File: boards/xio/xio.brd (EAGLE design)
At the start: 170 x 170 mm, 249 parts, among them CN3 J00-0065NL, U2 LAN8742A-CZ, X2 USB-A, Y1 NX3225SA-12.000MHZ-STD-CSR-1, Y2 NX3225SA-12.000MHZ-STD-CSR-1, Y3 NX3225SA-25.000MHZ-STD-CSR-1

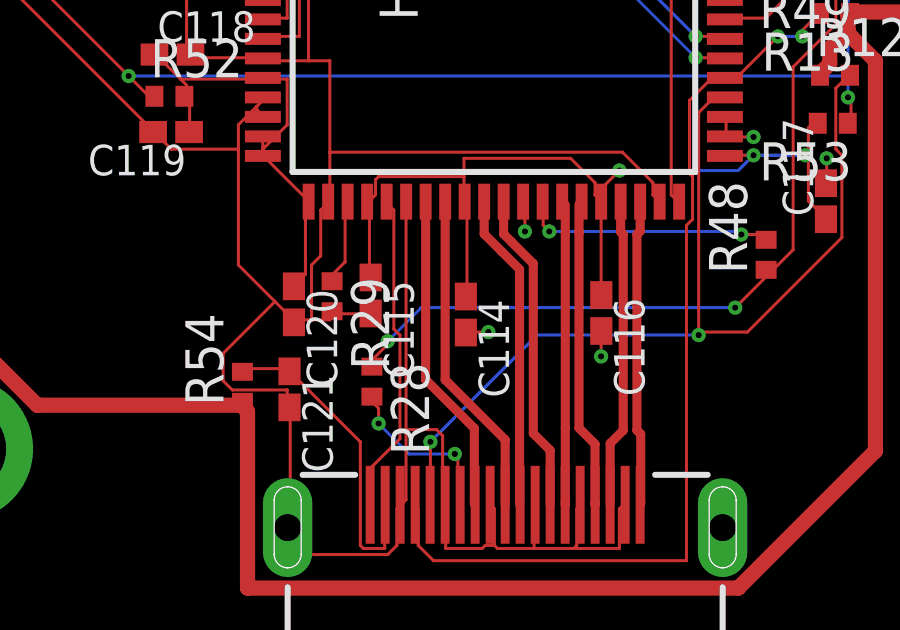
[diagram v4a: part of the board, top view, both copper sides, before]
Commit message: Re-route a diff-pair to be better matched
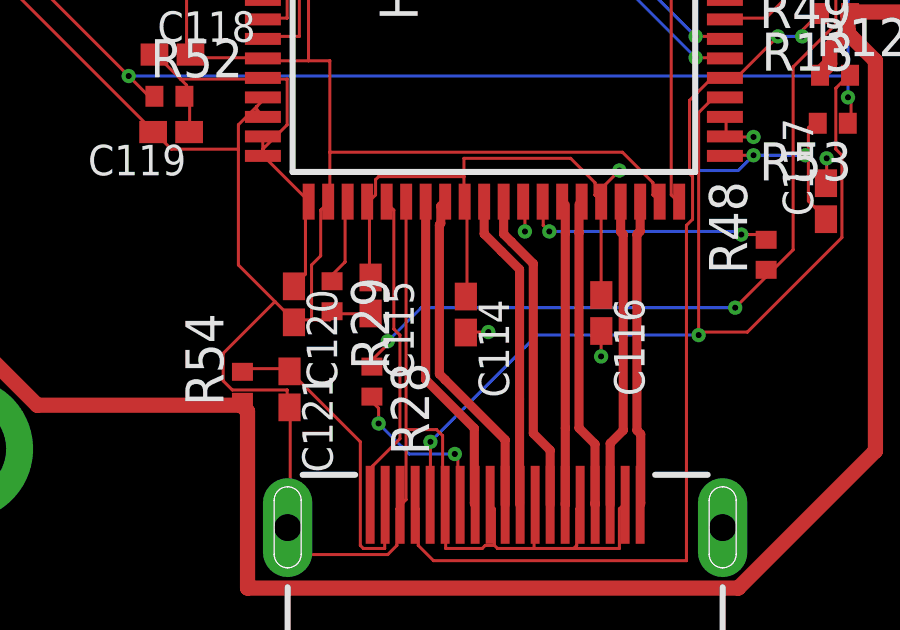
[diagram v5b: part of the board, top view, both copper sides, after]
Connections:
- net N$105 renamed XIO_RAM_A17
- net N$106 renamed XIO_RAM_A18
- net N$107 renamed XIO_RAM_D0
- net N$108 renamed XIO_RAM_D1
- net N$109 renamed XIO_RAM_D2
- net N$110 renamed XIO_RAM_D3
- net N$111 renamed XIO_RAM_D4
- net N$112 renamed XIO_RAM_D5
- net N$113 renamed XIO_RAM_D6
- net N$114 renamed XIO_RAM_D7
- net N$115 renamed XIO_RAM_D8
- net N$116 renamed XIO_RAM_D9
- net N$117 renamed XIO_RAM_D10
- net N$118 renamed XIO_RAM_D11
- net N$119 renamed XIO_RAM_D12
- net N$120 renamed XIO_RAM_D13
- net N$121 renamed XIO_RAM_D14
- net N$122 renamed XIO_RAM_D15
- net N$123 renamed XIO_RAM_!OE!
- net N$124 renamed XIO_RAM_!WE!
- net N$125 renamed XIO_RAM_!LB!
- net N$126 renamed XIO_RAM_!UB!
- net N$127 renamed XIO_RAM_!CS!
- net N$19 renamed XIO_RAM_A0
- net N$22 renamed XIO_RAM_A1
- net N$51 renamed XIO_RAM_A2
- net N$53 renamed XIO_RAM_A3
- net N$54 renamed XIO_RAM_A4
- net N$55 renamed XIO_RAM_A5
- net N$56 renamed XIO_RAM_A6
- net N$57 renamed XIO_RAM_A7
- net N$58 renamed XIO_RAM_A8
- net N$59 renamed XIO_RAM_A9
- net N$60 renamed XIO_RAM_A10
- net N$61 renamed XIO_RAM_A11
- net N$63 renamed XIO_RAM_A12
- net N$65 renamed XIO_RAM_A13
- net N$66 renamed XIO_RAM_A14
- net N$72 renamed XIO_RAM_A15
- net N$73 renamed XIO_RAM_A16

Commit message: Last minute changes prior to review
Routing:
- net +5V: vias 76 -> 92
- added copper zone on layer 1, net +5V
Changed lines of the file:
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@@
 <setting verticaltext="up"/>
 </settings>
-<grid distance="1" unitdist="mil" unit="mil" style="lines" multiple="1" display="yes" altdistance="5" altunitdist="mil" altunit="mil"/>
+<grid distance="0.025" unitdist="inch" unit="inch" style="lines" multiple="1" display="yes" altdistance="5" altunitdist="mil" altunit="mil"/>
 <layers>
 <layer number="1" name="Top" color="4" fill="1" visible="yes" active="yes"/>
@@
 <wire x1="49.5808" y1="84.4296" x2="49.53" y2="84.42" width="0.1016" layer="1"/>
 <wire x1="58.42" y1="84.4296" x2="58.42" y2="84.42" width="0.1016" layer="1"/>
-<wire x1="36.9824" y1="8.7376" x2="36.8808" y2="8.8392" width="0.1016" layer="1"/>
-<wire x1="36.9824" y1="7.5184" x2="36.9824" y2="8.7376" width="0.1016" layer="1"/>
-<wire x1="37.084" y1="7.4168" x2="36.9824" y2="7.5184" width="0.1016" layer="1"/>
-<wire x1="38.3032" y1="7.4168" x2="37.084" y2="7.4168" width="0.1016" layer="1"/>
-<wire x1="38.3032" y1="8.8392" x2="38.3032" y2="7.4168" width="0.1016" layer="1"/>
+<wire x1="36.8808" y1="8.7376" x2="36.8808" y2="8.8392" width="0.1016" layer="1"/>
+<wire x1="36.8808" y1="7.5184" x2="36.8808" y2="8.7376" width="0.1016" layer="1"/>
+<wire x1="37.084" y1="7.3152" x2="36.8808" y2="7.5184" width="0.1016" layer="1"/>
+<wire x1="38.3032" y1="7.3152" x2="37.084" y2="7.3152" width="0.1016" layer="1"/>
+<wire x1="38.3032" y1="8.8392" x2="38.3032" y2="7.3152" width="0.1016" layer="1"/>
 <wire x1="36.8808" y1="8.8392" x2="36.8399" y2="8.8721" width="0.1016" layer="1"/>
 <wire x1="38.3032" y1="8.8392" x2="38.3399" y2="8.8721" width="0.1016" layer="1"/>
-<wire x1="39.7256" y1="8.7376" x2="39.8272" y2="8.8392" width="0.1016" layer="1"/>
-<wire x1="39.7256" y1="7.5184" x2="39.7256" y2="8.7376" width="0.1016" layer="1"/>
-<wire x1="39.624" y1="7.4168" x2="39.7256" y2="7.5184" width="0.1016" layer="1"/>
-<wire x1="38.3032" y1="7.4168" x2="39.624" y2="7.4168" width="0.1016" layer="1"/>
+<wire x1="39.8272" y1="8.7376" x2="39.8272" y2="8.8392" width="0.1016" layer="1"/>
+<wire x1="39.8272" y1="7.5184" x2="39.8272" y2="8.7376" width="0.1016" layer="1"/>
+<wire x1="39.8272" y1="7.3152" x2="39.8272" y2="7.5184" width="0.1016" layer="1"/>
+<wire x1="38.3032" y1="7.3152" x2="39.8272" y2="7.3152" width="0.1016" layer="1"/>
 <wire x1="39.8272" y1="8.8392" x2="39.8399" y2="8.8721" width="0.1016" layer="1"/>
-<wire x1="41.148" y1="8.7376" x2="41.2496" y2="8.8392" width="0.1016" layer="1"/>
-<wire x1="41.148" y1="7.4168" x2="41.148" y2="8.7376" width="0.1016" layer="1"/>
-<wire x1="39.624" y1="7.4168" x2="41.148" y2="7.4168" width="0.1016" layer="1"/>
+<wire x1="41.2496" y1="8.7376" x2="41.2496" y2="8.8392" width="0.1016" layer="1"/>
+<wire x1="41.2496" y1="7.3152" x2="41.2496" y2="8.7376" width="0.1016" layer="1"/>
+<wire x1="39.8272" y1="7.3152" x2="41.2496" y2="7.3152" width="0.1016" layer="1"/>
 <wire x1="41.2496" y1="8.8392" x2="41.3399" y2="8.8721" width="0.1016" layer="1"/>
 <wire x1="34.036" y1="9.0424" x2="34.036" y2="11.3792" width="0.1016" layer="1"/>
@@
 <wire x1="34.036" y1="11.3792" x2="35.052" y2="11.3792" width="0.1016" layer="1"/>
 <wire x1="35.2552" y1="8.9408" x2="35.3399" y2="8.8721" width="0.1016" layer="1"/>
-<wire x1="36.6776" y1="7.5184" x2="36.9824" y2="7.5184" width="0.1016" layer="1"/>
-<wire x1="36.576" y1="7.4168" x2="36.6776" y2="7.5184" width="0.1016" layer="1"/>
-<wire x1="35.3568" y1="7.4168" x2="36.576" y2="7.4168" width="0.1016" layer="1"/>
-<wire x1="35.3568" y1="8.8392" x2="35.3568" y2="7.4168" width="0.1016" layer="1"/>
+<wire x1="36.7792" y1="7.5184" x2="36.8808" y2="7.5184" width="0.1016" layer="1"/>
+<wire x1="36.576" y1="7.3152" x2="36.7792" y2="7.5184" width="0.1016" layer="1"/>
+<wire x1="35.3568" y1="7.3152" x2="36.576" y2="7.3152" width="0.1016" layer="1"/>
+<wire x1="35.3568" y1="8.8392" x2="35.3568" y2="7.3152" width="0.1016" layer="1"/>
 <wire x1="35.3568" y1="8.8392" x2="35.3399" y2="8.8721" width="0.1016" layer="1"/>
 <wire x1="147.1168" y1="30.5816" x2="147.6248" y2="31.0896" width="0.1016" layer="1"/>
@@
 <via x="54.0512" y="25.2984" extent="1-16" drill="0.2"/>
 <via x="19.2024" y="49.6824" extent="1-16" drill="0.2"/>
+<polygon width="0.508" layer="1">
+<vertex x="1.905" y="45.085"/>
+<vertex x="12.065" y="45.085"/>
+<vertex x="12.065" y="70.485"/>
+<vertex x="1.905" y="70.485"/>
+</polygon>
+<via x="10.16" y="57.15" extent="1-16" drill="0.4" locked="yes"/>
+<via x="10.16" y="60.96" extent="1-16" drill="0.4" locked="yes"/>
+<via x="10.16" y="64.135" extent="1-16" drill="0.4" locked="yes"/>
+<via x="10.16" y="67.31" extent="1-16" drill="0.4" locked="yes"/>
+<via x="6.985" y="67.31" extent="1-16" drill="0.4" locked="yes"/>
+<via x="6.985" y="64.135" extent="1-16" drill="0.4" locked="yes"/>
+<via x="6.985" y="60.96" extent="1-16" drill="0.4" locked="yes"/>
+<via x="6.985" y="57.15" extent="1-16" drill="0.4" locked="yes"/>
+<via x="3.81" y="57.15" extent="1-16" drill="0.4" locked="yes"/>
+<via x="3.81" y="60.96" extent="1-16" drill="0.4" locked="yes"/>
+<via x="3.81" y="64.135" extent="1-16" drill="0.4" locked="yes"/>
+<via x="3.81" y="67.31" extent="1-16" drill="0.4" locked="yes"/>
+<via x="3.81" y="46.99" extent="1-16" drill="0.4" locked="yes"/>
+<via x="3.81" y="49.53" extent="1-16" drill="0.4" locked="yes"/>
+<via x="3.81" y="52.07" extent="1-16" drill="0.4" locked="yes"/>
+<via x="3.81" y="54.61" extent="1-16" drill="0.4" locked="yes"/>
 </signal>
 <signal name="!RESET!">
@@
 <wire x1="36.312753125" y1="11.420753125" x2="36.312753125" y2="8.9408" width="0.3048" layer="1" locked="yes"/>
 <wire x1="36.312753125" y1="8.9408" x2="36.312753125" y2="8.899246875" width="0.3048" layer="1" locked="yes"/>
-<wire x1="36.3728" y1="8.9408" x2="36.3399" y2="8.8721" width="0.1016" layer="1"/>
 <wire x1="36.3728" y1="8.9408" x2="36.312753125" y2="8.9408" width="0.1016" layer="1"/>
 <wire x1="36.312753125" y1="11.420753125" x2="34.6899" y2="13.04360625" width="0.3048" layer="1" locked="yes"/>
 <wire x1="34.6899" y1="13.04360625" x2="34.6899" y2="18.9771" width="0.3048" layer="1" locked="yes"/>
+<wire x1="36.3399" y1="8.8721" x2="36.3728" y2="8.8721" width="0.3048" layer="1"/>
+<wire x1="36.3728" y1="8.8721" x2="36.3728" y2="8.9408" width="0.3048" layer="1" locked="yes"/>
 </signal>
 <signal name="TX0_P">

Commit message: Part-way through the revisions after the schematic review
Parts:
- removed I2C_EXT: (no value), pinhead:1X04
- removed SPI_EXT_0, SPI_EXT_1, SPI_EXT_2: (no value), pinhead:1X05
- added C109, C134, C35, C36, C51, C53, C54, C55, C56, C81, C82, C84, C85, C86, C87, C99: 0.1uF, rcl:C0402K
- added C52: 4.7uF, rcl:C0402K
- added C83: 10uF, rcl:C0402K
- added I2C_EXT0, I2C_EXT1: (no value), pinhead:1X04
- added L1, L2, L3: BLM15EG221SN1D, inductors:0402
- added R21, R26, R27, R30, R31: 33, rcl:R0402
- added R55, R56: 0R, rcl:R0402
- added R58, R59, R83, R84, R85, R86, R87, R88: 0, rcl:R0402
- added SPI_EXT0, SPI_EXT1, SPI_EXT2: (no value), pinhead:2X04
- R51, R52: value 0R -> 33
- moved R51 78.5 mm to (107.6, 84.1), turned to 270 degrees
- moved R52 76.1 mm to (98.1, 47.3), turned to 90 degrees
- moved R53 67.3 mm to (110.5, 47.3), turned to 90 degrees
- moved C117 2.39 mm to (48.3, 21.4), turned to 180 degrees
- moved R48 1.80 mm to (44.8, 15.9)
- moved R62 1.44 mm to (43.2, 149.4), turned to 90 degrees
- moved C34 1.42 mm to (119.4, 72.5)
- moved C19 1.14 mm to (137.2, 50.8), turned to 0 degrees
- moved R65 1.11 mm to (102.9, 149.2), turned to 90 degrees
- moved R67 1.11 mm to (142.9, 149.2), turned to 90 degrees
- moved R63 1.11 mm to (63.2, 149.2), turned to 90 degrees
- moved C13 1.02 mm to (119.4, 71.4)
- moved R64 0.86 mm to (82.9, 149.5), turned to 90 degrees
- moved C9 0.80 mm to (83.1, 55.1), turned to 90 degrees
- moved C18 0.79 mm to (83.1, 57.7), turned to 270 degrees
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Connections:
- net N$10 renamed XIO_RX
- net N$21 renamed AUDIO_DATA
- net N$25 renamed AUDIO_SCLK
- net N$37 renamed AUDIO_WORD
- net N$7 renamed XIO_SWDIO
- net N$8 renamed XIO_SWDCLK
- net N$9 renamed XIO_TX
- removed net N$64: R57.1, STM_DBG2.C
- removed net N$67: PIO.113, STM_DBG2.A
- new net N$10: C38.1, R58.2, V33_0.P$3
- new net N$19: LED3.A, R4.2
- new net N$21: R52.2, XIO.177
- new net N$22: R22.1, STM_DBG1.A
- new net N$25: C40.1, R59.2, V33_1.P$3
- new net N$37: C42.1, R83.2, V33_2.P$3
- new net N$51: R57.1, STM_DBG2.A
- new net N$53: C44.1, R84.2, V33_3.P$3
- new net N$54: C46.1, R85.2, V33_4.P$3
- new net N$55: C48.1, R86.2, V33_5.P$3
- new net N$56: C50.1, R87.2, V33_6.P$3
- new net N$58: C107.1, C108.1, R88.2, VRE18.P$3
- new net N$7: R53.2, XIO.203
- new net N$8: PIO.203, R55.2
- new net N$9: C12.1, R56.2, VREG33.P$3
- new net XIO_VDDA: R21.1, XIO.42
- net +3V3: now also C134.2, C52.1, I2C_EXT0.1, I2C_EXT1.1, R19.2, R2.1, R21.2, R22.2, R3.1, R4.1, R53.1, R55.1, R56.1, R57.2, SPI_EXT0.4, SPI_EXT1.4, SPI_EXT2.4; no longer C12.1, PIO.203, VREG33.P$3, XIO.203, XIO.42
- net +5V: now also C35.1, C36.1, C51.1, C53.1, C54.1, C55.1, C56.1, C81.1, C82.1, C83.1
- net 1.8V: now also C84.2, C86.2, C99.2, L1.1, L2.1, L3.1, R88.1; no longer C107.1, C108.1, R51.1, R52.1, R53.1, VRE18.P$3
- net AGND: now also C1.2, C13.2, C57.2, C58.2
- net AVDD_9889B: now also C109.2, L3.2; no longer R53.2
- net DVDD_9889B: now also C85.2, L1.2; no longer R51.2
- net GND: now also C109.1, C134.1, C35.2, C36.2, C51.2, C52.2, C53.2, C54.2, C55.2, C56.2, C81.2, C82.2, C83.2, C84.1, C85.1, C86.1, C87.1, C99.1, I2C_EXT0.4, I2C_EXT1.4, R26.2, R27.2, R30.2, R31.1, SPI_EXT0.8, SPI_EXT1.8, SPI_EXT2.8; no longer C1.2, C13.2, C57.2, C58.2, R19.2, R2.2, R22.2, R3.2, R4.2, R57.2
- net I2C_SCL: now also I2C_EXT0.2, I2C_EXT1.2; no longer I2C_EXT.1, I2C_EXT.3
- net I2C_SDA: now also I2C_EXT0.3, I2C_EXT1.3; no longer I2C_EXT.2, I2C_EXT.4
- net N$12: now also LED1.A, R2.2; no longer LED3.A, XIO.172
- net N$13: now also LED1.C, XIO.166; no longer LED2.A, XIO.167
- net N$14: now also LED2.C, XIO.167; no longer LED1.A, XIO.166
- net N$15: now also LED3.C, XIO.172; no longer LED1.C, R4.1
- net N$16: now also LED2.A, R3.2; no longer LED2.C, R3.1
- net N$17: now also STM_DBG0.C; no longer STM_DBG0.A
- net N$18: now also R51.2, XIO.65; no longer LED3.C, R2.1
- net N$20: now also R19.1, STM_DBG0.A; no longer PIO.112, STM_DBG1.A
- net N$26: now also PIO.112; no longer R22.1
- net N$27: now also PIO.113, STM_DBG2.C; no longer R19.1, STM_DBG0.C
- net PVDD_9889B: now also C87.2, L2.2; no longer R52.2
- net S1_V33: now also R58.1; no longer C38.1, V33_0.P$3
- net S2_V33: now also R59.1; no longer C40.1, V33_1.P$3
- net S3_V33: now also R83.1; no longer C42.1, V33_2.P$3
- net S4_V33: now also R84.1; no longer C44.1, V33_3.P$3
- net S5_V33: now also R85.1; no longer C46.1, V33_4.P$3
- net S6_V33: now also R86.1; no longer C48.1, V33_5.P$3
- net S7_V33: now also R87.1; no longer C50.1, V33_6.P$3
- net SPI_CLK: now also R26.1, SPI_EXT0.1, SPI_EXT1.1, SPI_EXT2.1; no longer SPI_EXT_0.1, SPI_EXT_1.1, SPI_EXT_2.1
- net SPI_IRQ7: now also SPI_EXT0.7; no longer SPI_EXT_0.4
- net SPI_IRQ8: now also SPI_EXT1.7; no longer SPI_EXT_1.4
- net SPI_IRQ9: now also SPI_EXT2.7; no longer SPI_EXT_2.4
- net SPI_MISO: now also R30.1, SPI_EXT0.3, SPI_EXT1.3, SPI_EXT2.3; no longer SPI_EXT_0.2, SPI_EXT_1.2, SPI_EXT_2.2
- net SPI_MOSI: now also R27.1, SPI_EXT0.5, SPI_EXT1.5, SPI_EXT2.5; no longer SPI_EXT_0.3, SPI_EXT_1.3, SPI_EXT_2.3
- net SPI_SS7: now also SPI_EXT0.6; no longer SPI_EXT_0.5
- net SPI_SS8: now also SPI_EXT1.6; no longer SPI_EXT_1.5
- net SPI_SS9: now also SPI_EXT2.6; no longer SPI_EXT_2.5
- net VHDCI_CLK: now also R31.2, R51.1; no longer XIO.65
- net VIDBUS_CLK: now also R52.1; no longer XIO.177
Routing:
- net +3V3: track 1051.5 -> 0.00 mm, vias 32 -> 0
- net GND: track 905.3 -> 0.00 mm, vias 69 -> 0
- net +5V: track 506.5 -> 127.4 mm, vias 92 -> 104
- net VHDCI_A11: track 365.4 -> 0.00 mm, vias 7 -> 0
- net VHDCI_A8: track 361.1 -> 0.00 mm, vias 4 -> 0
- net VHDCI_A6: track 356.4 -> 0.00 mm, vias 3 -> 0
- net VHDCI_AUDIO_R: track 356.0 -> 0.00 mm, vias 4 -> 0
- net VHDCI_AUDIO_SIO: track 348.6 -> 0.00 mm, vias 4 -> 0
- net I2C_SCL: track 347.5 -> 0.00 mm, vias 5 -> 0
- net VHDCI_D2: track 343.7 -> 0.00 mm, vias 4 -> 0
- net VHDCI_AUDIO_L: track 343.7 -> 0.00 mm, vias 5 -> 0
- net VHDCI_A12: track 340.8 -> 0.00 mm, vias 3 -> 0
- net VHDCI_A9: track 339.4 -> 0.00 mm, vias 3 -> 0
- net !VHDCI_IRQ!: track 331.0 -> 0.00 mm, vias 7 -> 0
- net VHDCI_D1XX: track 328.9 -> 0.00 mm, vias 10 -> 0
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
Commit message: Latest schematic/board after most things in the review completed
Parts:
- added C135: 120pF, rcl:C0402K
- added C136: 10nF, rcl:C0402K
- added C137: 0.1uF, rcl:C0402K
- added C138: 4.7uF, rcl:C0402K
- added R89, R90, R92: 10K, rcl:R0402
- added RESET_SW: (no value), SparkFun:TACTILE-PTH
- added U$3: TPS3808G33DBVR, sjg-power:SOT23-6
- moved XSPI2_TST 4.82 mm to (163.3, 84.6)
- moved XSP1_TST 3.93 mm to (6.90, 84.6), turned to 180 degrees
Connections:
- net N$128 renamed PIO_RX
- net N$129 renamed PIO_TX
- net N$130 renamed PIO_SWDCLK
- removed net N$131: PIO-SWD.P2, PIO.147
- new net !MR!: C136.1, RESET_SW.1, RESET_SW.2, U$3.3
- new net N$60: C135.1, U$3.4
- new net PIO_SWDIO: PIO-SWD.P2, PIO.147, R92.2
- net !RESET!: now also R89.2, U$3.1
- net +3V3: now also C137.1, C138.1, R89.1, R90.1, R92.1, U$3.5, U$3.6
- net GND: now also C135.2, C136.2, C137.2, C138.2, RESET_SW.3, RESET_SW.4, U$3.2
- net XIO_SWDIO: now also R90.2
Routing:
- net +3V3: track 0.00 -> 1151.8 mm, vias 0 -> 33
- net GND: track 0.00 -> 879.4 mm, vias 0 -> 83
- net +5V: track 127.4 -> 540.4 mm, vias 104 -> 116
- net VHDCI_AUDIO_SIO: track 0.00 -> 359.8 mm, vias 0 -> 5
- net VHDCI_A9: track 0.00 -> 356.9 mm, vias 0 -> 4
- net VHDCI_A2: track 0.00 -> 352.0 mm, vias 0 -> 6
- net VHDCI_A12: track 0.00 -> 345.3 mm, vias 0 -> 3
- net VHDCI_AUDIO_L: track 0.00 -> 342.1 mm, vias 0 -> 4
- net VHDCI_AUDIO_R: track 0.00 -> 340.3 mm, vias 0 -> 3
- net I2C_SDA: track 0.00 -> 336.8 mm, vias 0 -> 3
- net !VHDCI_MPD!: track 0.00 -> 331.1 mm, vias 0 -> 3
- net VHDCI_D2: track 0.00 -> 330.3 mm, vias 0 -> 5
- net VHDCI_A11: track 0.00 -> 320.6 mm, vias 0 -> 10
- net VHDCI_REF: track 0.00 -> 316.4 mm, vias 0 -> 4
- net VHDCI_A10: track 0.00 -> 311.8 mm, vias 0 -> 3
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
